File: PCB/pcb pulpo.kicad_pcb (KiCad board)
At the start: 2 copper layers, 116.8 x 109.2 mm, 76 parts, among them J1 Fan1, J10 Fan10, J12 izq, J13 dcha, J14 inf, J2 Fan2, J3 Fan3, J4 Fan4, J5 Fan5, J6 Fan6, J7 Fan7, J8 Fan8, J9 Fan9, U1 Teensy3.2, U2 LM7805_TO220

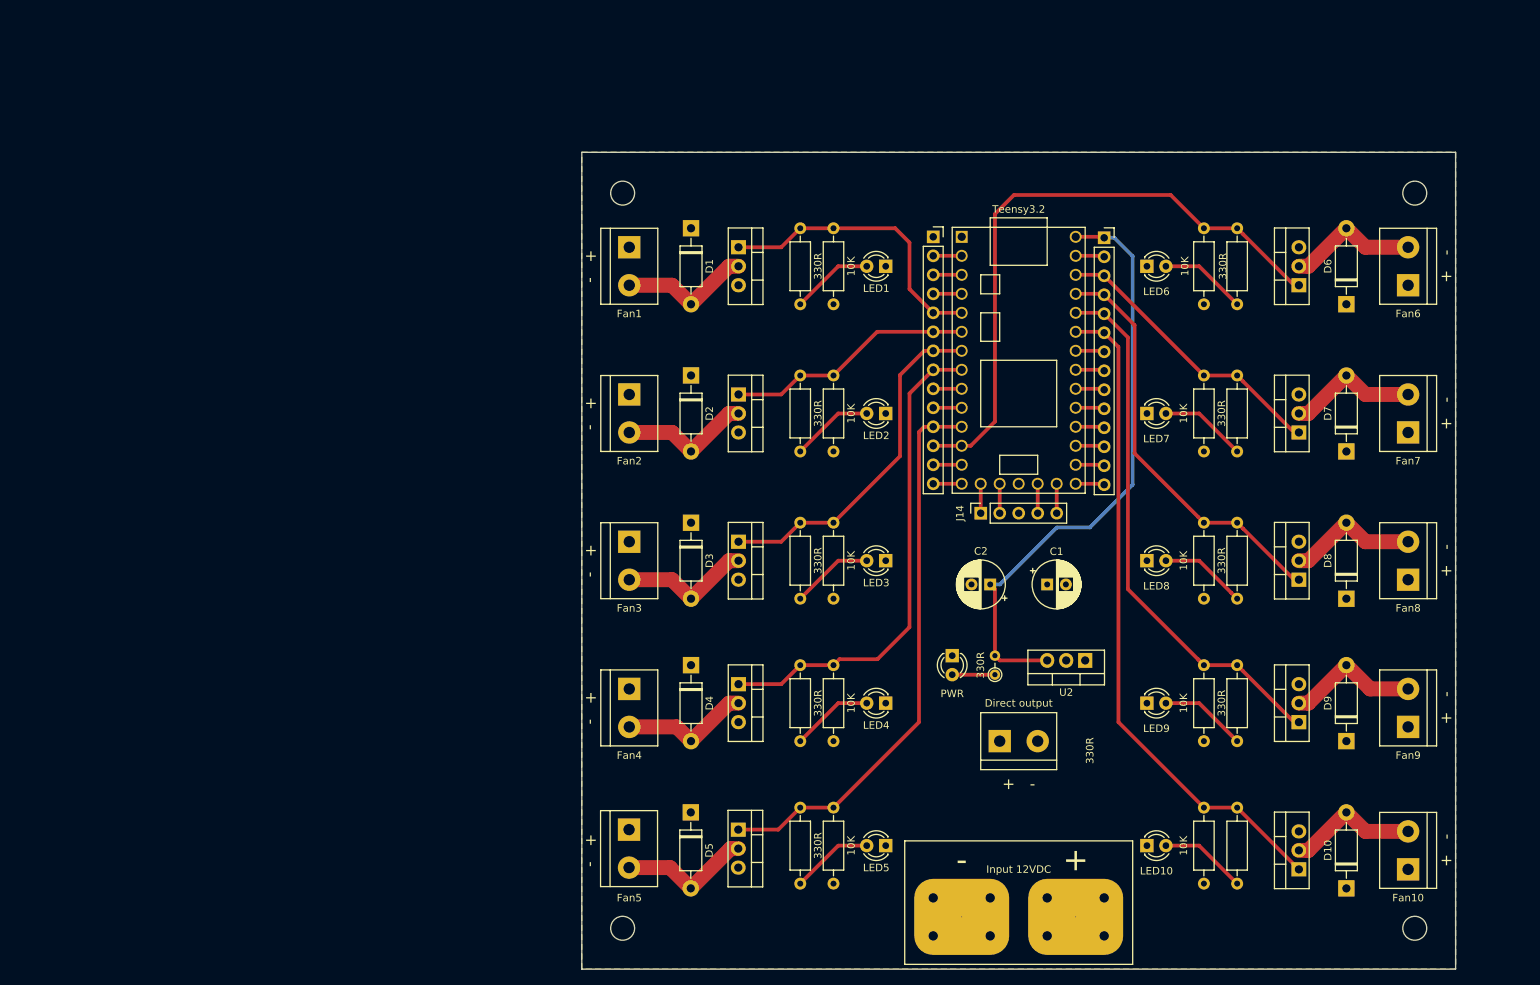
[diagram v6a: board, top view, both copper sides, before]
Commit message: Se añade logo de BricoLabs
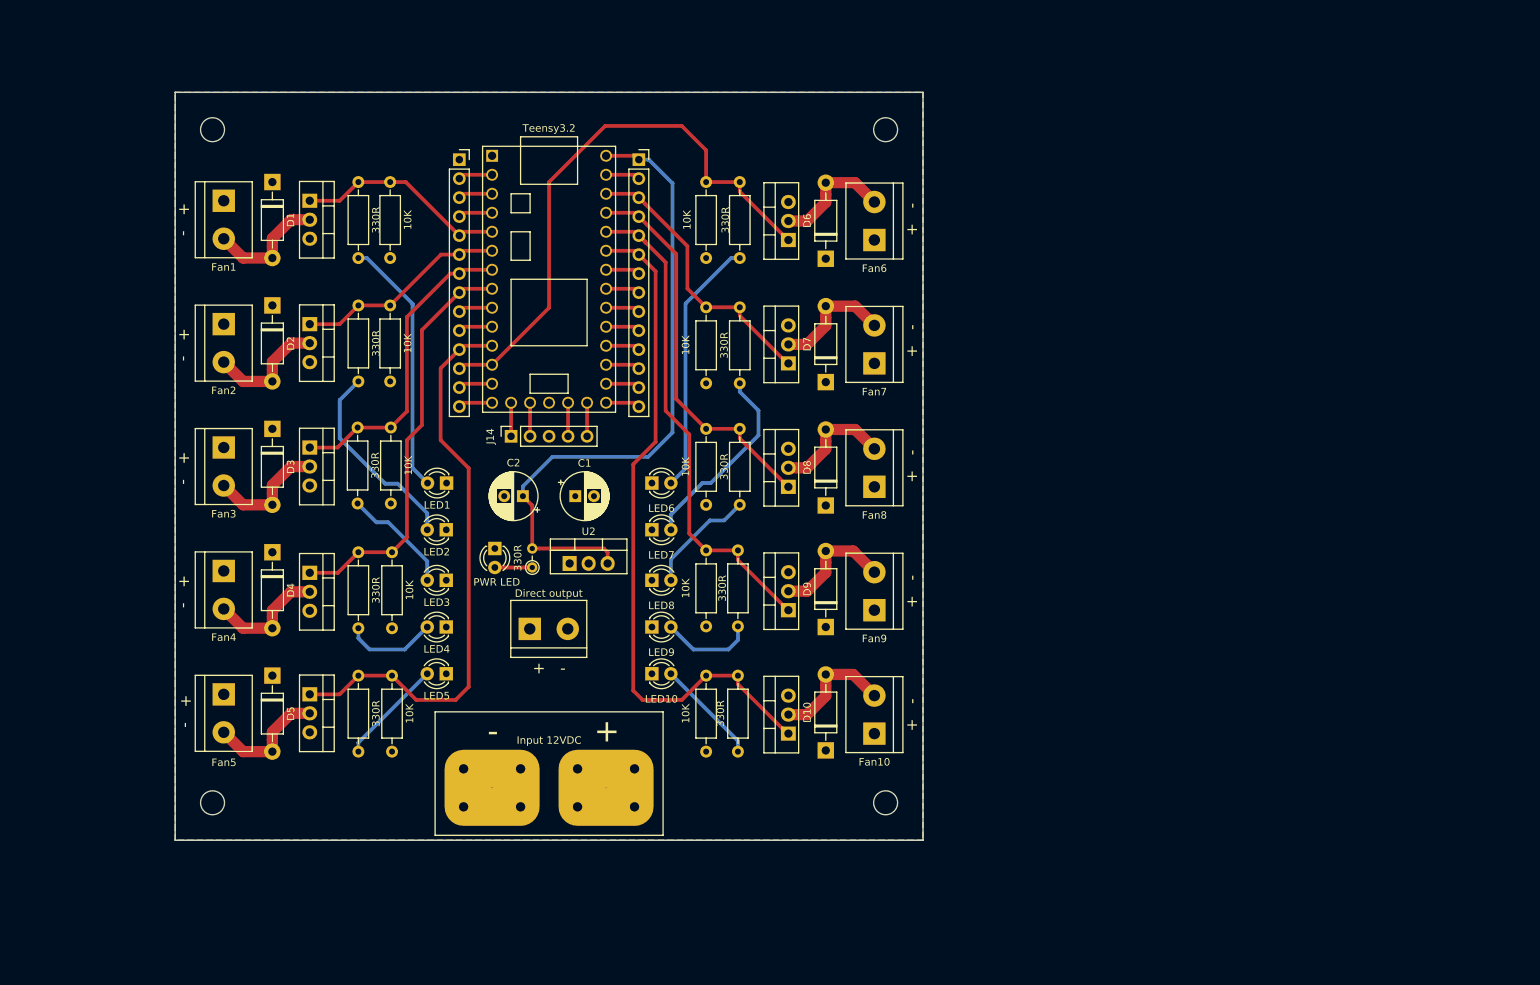
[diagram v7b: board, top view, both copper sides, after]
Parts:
- removed the 10K at (113.0, 82.5)
- removed the 10K at (113.0, 101.6)
- removed the 330R at (108.6, 82.5)
- removed the 330R at (108.6, 101.6)
- removed the 330R at (167.0, 62.9)
- removed the REF** at (190.8, 38.5)
- removed the REF** at (84.8, 38.5)
- added 10K: 10K, Resistor_THT:R_Axial_DIN0207_L6.3mm_D2.5mm_P10.16mm_Horizontal, F.Cu at (53.8, 69.8)
- added 10K: 10K, Resistor_THT:R_Axial_DIN0207_L6.3mm_D2.5mm_P10.16mm_Horizontal, F.Cu at (54.0, 86.5)
- added 330R: 330R, Resistor_THT:R_Axial_DIN0207_L6.3mm_D2.5mm_P10.16mm_Horizontal, F.Cu at (49.4, 69.8)
- added 330R: 330R, Resistor_THT:R_Axial_DIN0207_L6.3mm_D2.5mm_P10.16mm_Horizontal, F.Cu at (49.5, 86.5)
- added 330R: 330R, Resistor_THT:R_Axial_DIN0207_L6.3mm_D2.5mm_P10.16mm_Horizontal, F.Cu at (100.5, 53.8)
- added G***: LOGO, Logos:BricoLabs_logo_small, B.Cu at (75.0, 40.0)
- added REF**: MountingHole_3.2mm_M3, MountingHole:MountingHole_3.2mm_M3, F.Cu at (120.0, 30.0)
- added REF**: MountingHole_3.2mm_M3, MountingHole:MountingHole_3.2mm_M3, F.Cu at (30.0, 30.0)
- PWR LED: renamed from PWR
- moved J10 73.6 mm to (118.5, 110.8)
- moved J9 73.1 mm to (118.5, 94.2)
- moved REF** 72.7 mm to (120.0, 120.0)
- moved J8 72.4 mm to (118.5, 77.8)
- moved LED6 72.3 mm to (88.8, 77.2)
- moved D10 72.0 mm to (112.0, 113.0)
- moved J7 72.0 mm to (118.5, 61.2)
- moved J6 71.6 mm to (118.5, 44.8)
- moved D9 71.3 mm to (112.0, 96.5)
- moved D8 70.7 mm to (112.0, 80.2)
- moved MOS_10 70.6 mm to (107.0, 110.8)
- moved D7 70.2 mm to (112.0, 63.8)
- moved U2 70.1 mm to (77.8, 88.0), turned to 0 degrees
- moved LED10 70.1 mm to (88.8, 102.8)
- moved MOS_9 69.9 mm to (107.0, 94.2)
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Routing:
- net Net-(LED1-Pad2): track 11.0 -> 34.8 mm
- net Net-(LED6-Pad2): track 11.6 -> 34.6 mm
- net Net-(LED2-Pad2): track 11.0 -> 26.7 mm
- net Net-(LED7-Pad2): track 11.6 -> 26.1 mm
- net pin1: track 39.2 -> 28.6 mm
- net pin4: track 65.6 -> 55.2 mm
- net pin6: track 84.0 -> 76.9 mm
- net pin8: track 73.4 -> 66.8 mm
- net Net-(C2-Pad1): track 80.9 -> 87.3 mm
- net pin3: track 46.8 -> 41.6 mm
- net pin2: track 33.3 -> 28.4 mm
- net Net-(LED3-Pad2): track 11.0 -> 15.1 mm
- net pin9: track 55.7 -> 51.7 mm
- net Net-(LED8-Pad2): track 11.6 -> 15.0 mm
- net Net-(LED5-Pad2): track 11.0 -> 14.2 mm
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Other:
- board size 116.8 x 109.2 mm -> 100 x 100 mm
- net class Default: trace_width 0.5 -> 1.5
